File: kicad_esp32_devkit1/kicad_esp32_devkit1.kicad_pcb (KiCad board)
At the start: 2 copper layers, 30 parts, among them J1 Conn_01x03_Male, J10 Conn_01x04_Male, J11 Conn_01x04_Male, J12 Conn_01x04_Male, J13 Conn_01x04_Male, J14 Conn_01x04_Male, J15 Conn_01x04_Male, J16 Conn_01x04_Male, J17 Conn_01x04_Male, J18 Conn_01x04_Male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

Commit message: Reorganize Layout
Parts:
- moved J27 186.7 mm to (200.7, 88.9), turned to 180 degrees
- moved J26 137.7 mm to (175.3, 88.9), turned to 180 degrees
- moved J25 111.3 mm to (154.9, 47.0)
- moved J30 90.0 mm to (154.9, 110.5)
- moved J29 89.8 mm to (154.9, 97.8)
- moved J28 89.6 mm to (154.9, 85.1)
- moved J12 2.85 mm to (101.6, 110.5)
- moved J18 2.85 mm to (119.4, 110.5)
- moved J4 2.84 mm to (86.4, 85.1)
- moved J6 2.84 mm to (86.4, 110.5)
- moved J24 2.84 mm to (137.2, 110.5)
- moved J10 2.54 mm to (101.6, 85.1)
- moved J11 2.54 mm to (101.6, 97.8)
- moved J13 2.54 mm to (119.4, 47.0)
- moved J14 2.54 mm to (119.4, 59.7)
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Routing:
- net (no net): vias 0 -> 4
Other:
- net class Default removed

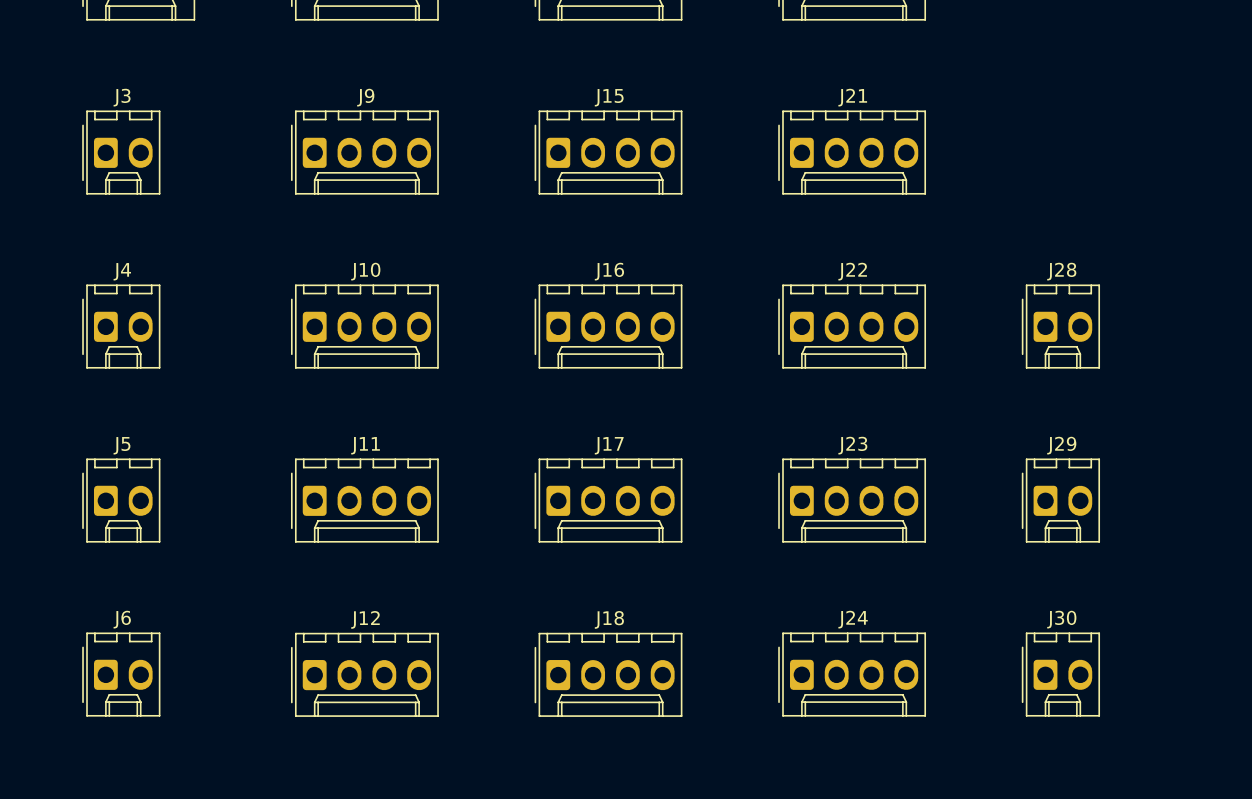
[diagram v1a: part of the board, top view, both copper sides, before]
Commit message: Reorganize Layout
Add schematics.
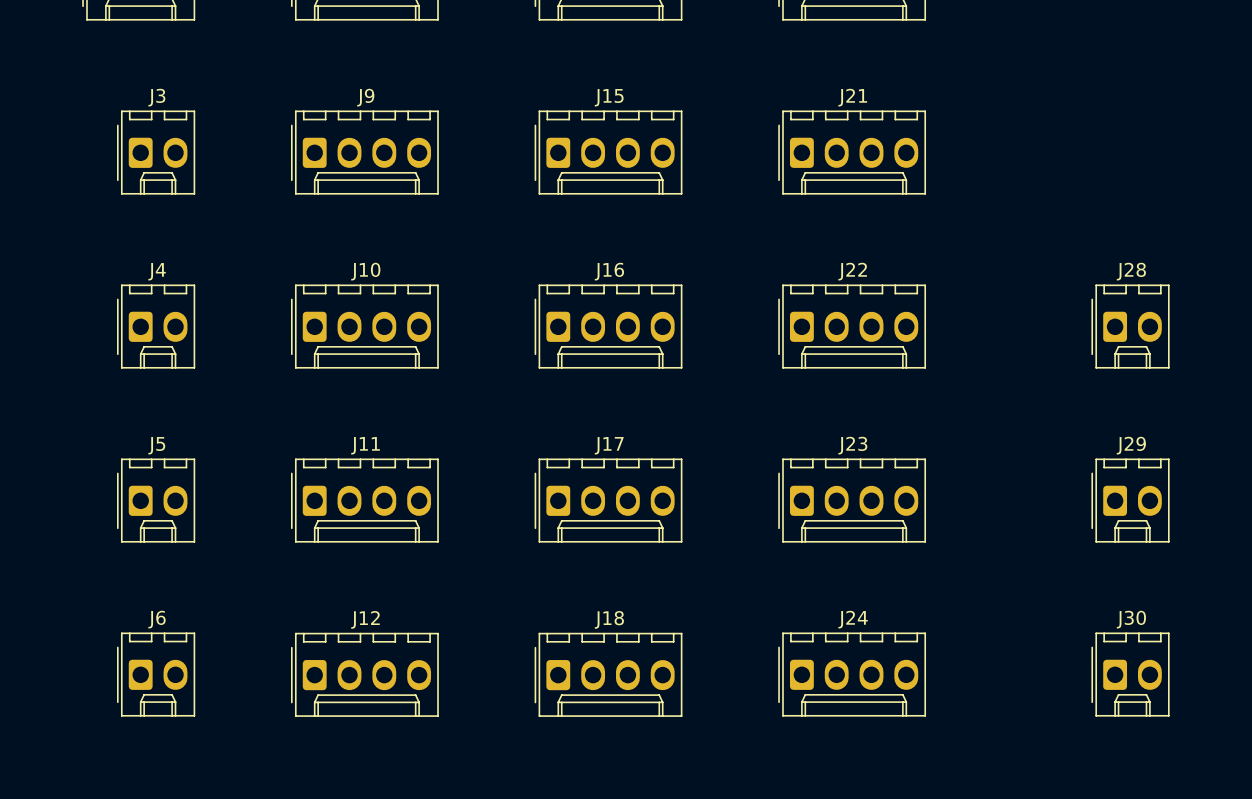
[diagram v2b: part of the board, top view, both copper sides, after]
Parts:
- moved J28 5.08 mm to (160.0, 85.1)
- moved J29 5.08 mm to (160.0, 97.8)
- moved J30 5.08 mm to (160.0, 110.5)
- moved J3 2.54 mm to (88.9, 72.4)
- moved J4 2.54 mm to (88.9, 85.1)
- moved J5 2.54 mm to (88.9, 97.8)
- moved J6 2.54 mm to (88.9, 110.5)
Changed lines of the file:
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@@
   )
   (footprint "Connector_Molex:Molex_KK-254_AE-6410-02A_1x02_P2.54mm_Vertical" (layer "F.Cu")
-    (at 86.36 72.39)
+    (at 88.9 72.39)
     (descr "Molex KK-254 Interconnect System, old/engineering part number: AE-6410-02A example for new part number: 22-27-2021, 2 Pins (http://www.molex.com/pdm_docs/sd/022272021_sd.pdf), generated with kicad-footprint-generator")
     (tags "connector Molex KK-254 side entry")
@@
       (effects (font (size 1 1) (thickness 0.15)))
     )
-    (fp_text value "Conn_01x02_Male" (at 2.54 4.08) (layer "F.Fab")
+    (fp_text value "Conn_01x02_Male" (at 0 4.08) (layer "F.Fab")
       (effects (font (size 1 1) (thickness 0.15)))
     )
@@
   )
   (footprint "Connector_Molex:Molex_KK-254_AE-6410-02A_1x02_P2.54mm_Vertical" (layer "F.Cu")
-    (at 86.36 85.09)
+    (at 88.9 85.09)
     (descr "Molex KK-254 Interconnect System, old/engineering part number: AE-6410-02A example for new part number: 22-27-2021, 2 Pins (http://www.molex.com/pdm_docs/sd/022272021_sd.pdf), generated with kicad-footprint-generator")
     (tags "connector Molex KK-254 side entry")
@@
       (effects (font (size 1 1) (thickness 0.15)))
     )
-    (fp_text value "Conn_01x02_Male" (at 1.27 4.08) (layer "F.Fab")
+    (fp_text value "Conn_01x02_Male" (at 0 4.08) (layer "F.Fab")
       (effects (font (size 1 1) (thickness 0.15)))
     )
@@
   )
   (footprint "Connector_Molex:Molex_KK-254_AE-6410-02A_1x02_P2.54mm_Vertical" (layer "F.Cu")
-    (at 86.36 97.79)
+    (at 88.9 97.79)
     (descr "Molex KK-254 Interconnect System, old/engineering part number: AE-6410-02A example for new part number: 22-27-2021, 2 Pins (http://www.molex.com/pdm_docs/sd/022272021_sd.pdf), generated with kicad-footprint-generator")
     (tags "connector Molex KK-254 side entry")
@@
       (effects (font (size 1 1) (thickness 0.15)))
     )
-    (fp_text value "Conn_01x02_Male" (at 1.27 4.08) (layer "F.Fab")
+    (fp_text value "Conn_01x02_Male" (at 0 4.08) (layer "F.Fab")
       (effects (font (size 1 1) (thickness 0.15)))
     )
@@
   )
   (footprint "Connector_Molex:Molex_KK-254_AE-6410-02A_1x02_P2.54mm_Vertical" (layer "F.Cu")
-    (at 86.36 110.49)
+    (at 88.9 110.49)
     (descr "Molex KK-254 Interconnect System, old/engineering part number: AE-6410-02A example for new part number: 22-27-2021, 2 Pins (http://www.molex.com/pdm_docs/sd/022272021_sd.pdf), generated with kicad-footprint-generator")
     (tags "connector Molex KK-254 side entry")
@@
       (effects (font (size 1 1) (thickness 0.15)))
     )
-    (fp_text value "Conn_01x02_Male" (at 1.27 4.08) (layer "F.Fab")
+    (fp_text value "Conn_01x02_Male" (at 0 4.08) (layer "F.Fab")
       (effects (font (size 1 1) (thickness 0.15)))
     )
@@
   )
   (footprint "Connector_Molex:Molex_KK-254_AE-6410-02A_1x02_P2.54mm_Vertical" (layer "F.Cu")
-    (at 154.94 85.09)
+    (at 160.02 85.09)
     (descr "Molex KK-254 Interconnect System, old/engineering part number: AE-6410-02A example for new part number: 22-27-2021, 2 Pins (http://www.molex.com/pdm_docs/sd/022272021_sd.pdf), generated with kicad-footprint-generator")
     (tags "connector Molex KK-254 side entry")
@@
       (effects (font (size 1 1) (thickness 0.15)))
     )
-    (fp_text value "Conn_01x02_Male" (at 1.27 4.08) (layer "F.Fab")
+    (fp_text value "Conn_01x02_Male" (at -1.27 4.08) (layer "F.Fab")
       (effects (font (size 1 1) (thickness 0.15)))
     )
@@
   )
   (footprint "Connector_Molex:Molex_KK-254_AE-6410-02A_1x02_P2.54mm_Vertical" (layer "F.Cu")
-    (at 154.94 97.79)
+    (at 160.02 97.79)
     (descr "Molex KK-254 Interconnect System, old/engineering part number: AE-6410-02A example for new part number: 22-27-2021, 2 Pins (http://www.molex.com/pdm_docs/sd/022272021_sd.pdf), generated with kicad-footprint-generator")
     (tags "connector Molex KK-254 side entry")
@@
       (effects (font (size 1 1) (thickness 0.15)))
     )
-    (fp_text value "Conn_01x02_Male" (at 1.27 4.08) (layer "F.Fab")
+    (fp_text value "Conn_01x02_Male" (at -1.27 4.08) (layer "F.Fab")
       (effects (font (size 1 1) (thickness 0.15)))
     )
@@
   )
   (footprint "Connector_Molex:Molex_KK-254_AE-6410-02A_1x02_P2.54mm_Vertical" (layer "F.Cu")
-    (at 154.94 110.49)
+    (at 160.02 110.49)
     (descr "Molex KK-254 Interconnect System, old/engineering part number: AE-6410-02A example for new part number: 22-27-2021, 2 Pins (http://www.molex.com/pdm_docs/sd/022272021_sd.pdf), generated with kicad-footprint-generator")
     (tags "connector Molex KK-254 side entry")
@@
       (effects (font (size 1 1) (thickness 0.15)))
     )
-    (fp_text value "Conn_01x02_Male" (at 1.27 4.08) (layer "F.Fab")
-      (effects (font (size 1 1) (thickness 0.15)))
-    )
+    (fp_text value "Conn_01x02_Male" (at -1.27 4.08) (layer "F.Fab")
+      (effects (font (size 1 1) (thickness 0.15)))
+    )
